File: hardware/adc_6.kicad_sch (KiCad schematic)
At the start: 12 parts, among them J5 Conn_01x04, U5 ADS122C04IPW

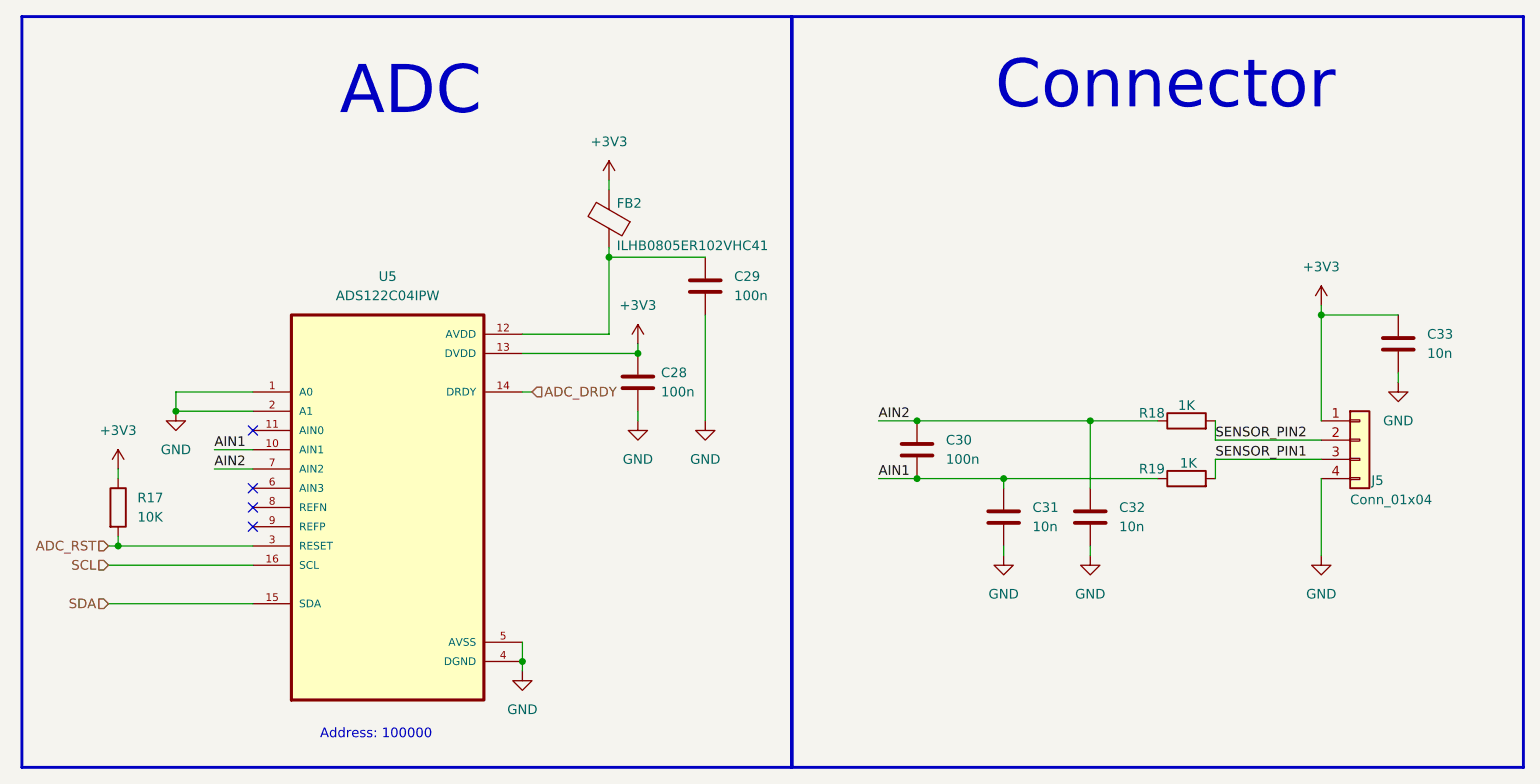
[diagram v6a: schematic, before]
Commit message: Route Ethernet section and add global labels
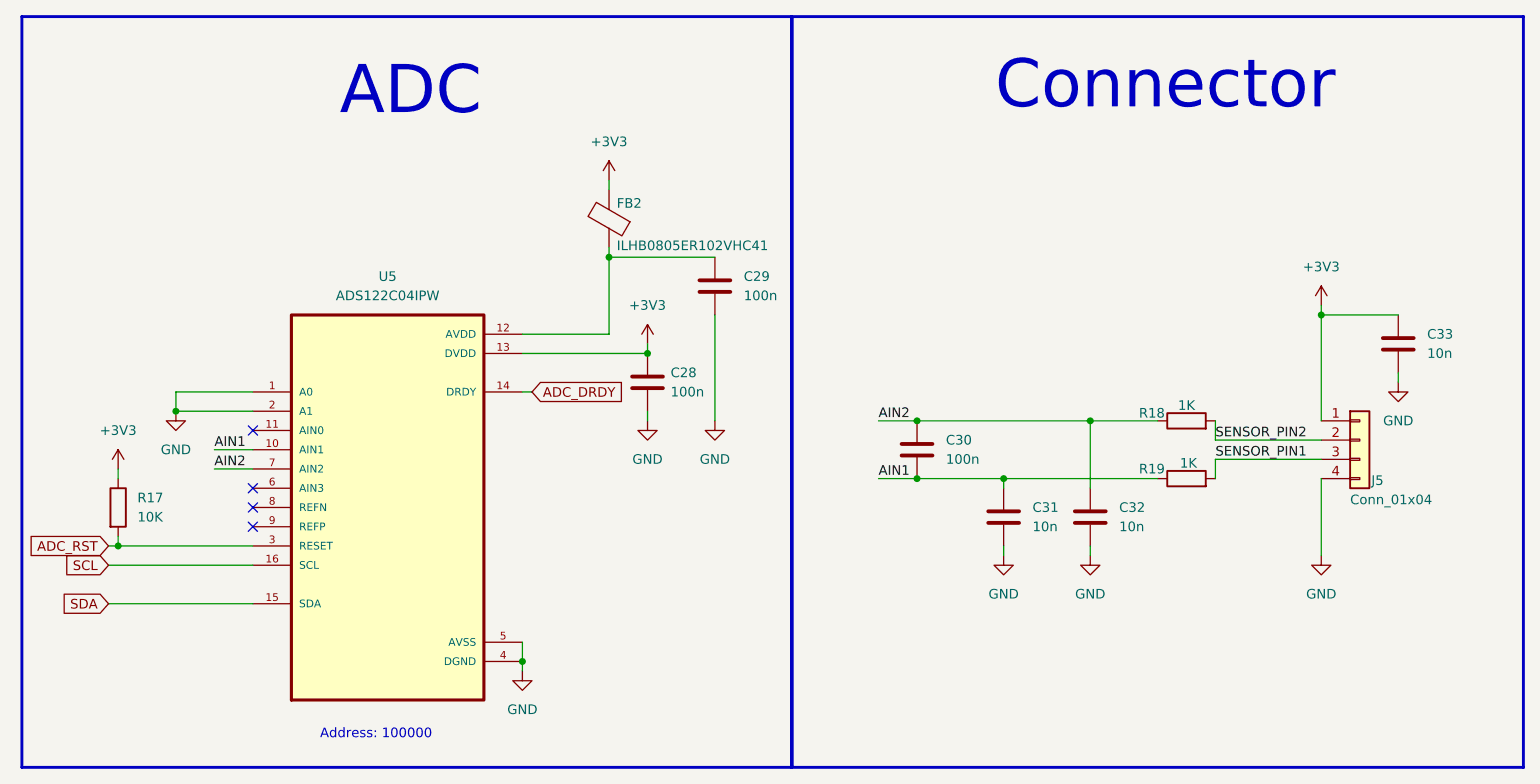
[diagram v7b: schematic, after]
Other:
- moved on the sheet: C28, C29
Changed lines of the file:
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@@
 	)
 	(junction
-		(at 132.08 86.36)
+		(at 133.35 86.36)
 		(diameter 0)
 		(color 0 0 0 0)
@@
 	(wire
 		(pts
-			(xy 116.84 86.36) (xy 132.08 86.36)
+			(xy 116.84 86.36) (xy 133.35 86.36)
 		)
 		(stroke
@@
 	(wire
 		(pts
-			(xy 132.08 95.25) (xy 132.08 93.98)
+			(xy 133.35 95.25) (xy 133.35 93.98)
 		)
 		(stroke
@@
 	(wire
 		(pts
-			(xy 128.27 73.66) (xy 140.97 73.66)
+			(xy 128.27 73.66) (xy 142.24 73.66)
 		)
 		(stroke
@@
 	(wire
 		(pts
-			(xy 140.97 95.25) (xy 140.97 81.28)
+			(xy 142.24 95.25) (xy 142.24 81.28)
 		)
 		(stroke
@@
 	(wire
 		(pts
-			(xy 132.08 85.09) (xy 132.08 86.36)
+			(xy 133.35 85.09) (xy 133.35 86.36)
 		)
 		(stroke
@@
 		)
 	)
-	(hierarchical_label "SCL"
+	(global_label "ADC_DRDY"
 		(shape input)
-		(at 62.23 114.3 180)
+		(at 118.11 91.44 0)
+		(fields_autoplaced yes)
 		(effects
 			(font
 				(size 1.27 1.27)
 			)
-			(justify right)
-		)
-	)
-	(hierarchical_label "ADC_DRDY"
+			(justify left)
+		)
+		(property "Intersheetrefs" "${INTERSHEET_REFS}"
+			(at 130.59 91.44 0)
+			(hide yes)
+			(show_name no)
+			(do_not_autoplace no)
+			(effects
+				(font
+					(size 1.27 1.27)
+				)
+				(justify left)
+			)
+		)
+	)
+	(global_label "SDA"
 		(shape input)
-		(at 118.11 91.44 0)
+		(at 62.23 119.38 180)
+		(fields_autoplaced yes)
 		(effects
 			(font
 				(size 1.27 1.27)
 			)
-			(justify left)
-		)
-	)
-	(hierarchical_label "SDA"
+			(justify right)
+		)
+		(property "Intersheetrefs" "${INTERSHEET_REFS}"
+			(at 55.6767 119.38 0)
+			(hide yes)
+			(show_name no)
+			(do_not_autoplace no)
+			(effects
+				(font
+					(size 1.27 1.27)
+				)
+				(justify right)
+			)
+		)
+	)
+	(global_label "SCL"
 		(shape input)
-		(at 62.23 119.38 180)
+		(at 62.23 114.3 180)
+		(fields_autoplaced yes)
 		(effects
 			(font
@@
 			(justify right)
 		)
-	)
-	(hierarchical_label "ADC_RST"
+		(property "Intersheetrefs" "${INTERSHEET_REFS}"
+			(at 55.7372 114.3 0)
+			(hide yes)
+			(show_name no)
+			(do_not_autoplace no)
+			(effects
+				(font
+					(size 1.27 1.27)
+				)
+				(justify right)
+			)
+		)
+	)
+	(global_label "ADC_RST"
 		(shape input)
 		(at 62.23 111.76 180)
+		(fields_autoplaced yes)
 		(effects
 			(font
@@
 			)
 			(justify right)
+		)
+		(property "Intersheetrefs" "${INTERSHEET_REFS}"
+			(at 51.2015 111.76 0)
+			(hide yes)
+			(show_name no)
+			(do_not_autoplace no)
+			(effects
+				(font
+					(size 1.27 1.27)
+				)
+				(justify right)
+			)
 		)
 	)
@@
 	(symbol
 		(lib_id "power:GND")
-		(at 132.08 95.25 0)
+		(at 133.35 95.25 0)
 		(unit 1)
 		(body_style 1)
@@
 		(fields_autoplaced yes)
 		(property "Reference" "#PWR056"
-			(at 132.08 101.6 0)
+			(at 133.35 101.6 0)
 			(hide yes)
 			(show_name no)
@@
 		)
 		(property "Value" "GND"
-			(at 132.08 100.33 0)
+			(at 133.35 100.33 0)
 			(show_name no)
 			(do_not_autoplace no)
@@
 		)
 		(property "Footprint" ""
-			(at 132.08 95.25 0)
+			(at 133.35 95.25 0)
 			(hide yes)
 			(show_name no)
@@
 		)
 		(property "Datasheet" ""
-			(at 132.08 95.25 0)
+			(at 133.35 95.25 0)
 			(hide yes)
 			(show_name no)
@@
 		)
 		(property "Description" "Power symbol creates a global label with name \"GND\" , ground"
-			(at 132.08 95.25 0)
+			(at 133.35 95.25 0)
 			(hide yes)
 			(show_name no)
@@
 	(symbol
 		(lib_id "power:+3V3")
-		(at 132.08 85.09 0)
+		(at 133.35 85.09 0)
 		(unit 1)
 		(body_style 1)
@@
 		(fields_autoplaced yes)
 		(property "Reference" "#PWR055"
-			(at 132.08 88.9 0)
+			(at 133.35 88.9 0)
 			(hide yes)
 			(show_name no)
@@
 		)
 		(property "Value" "+3V3"
-			(at 132.08 80.01 0)
+			(at 133.35 80.01 0)
 			(show_name no)
 			(do_not_autoplace no)
@@
 		)
 		(property "Footprint" ""
-			(at 132.08 85.09 0)
+			(at 133.35 85.09 0)
 			(hide yes)
 			(show_name no)
@@
 		)
 		(property "Datasheet" ""
-			(at 132.08 85.09 0)
+			(at 133.35 85.09 0)
 			(hide yes)
 			(show_name no)
@@
 		)
 		(property "Description" "Power symbol creates a global label with name \"+3V3\""
-			(at 132.08 85.09 0)
+			(at 133.35 85.09 0)
 			(hide yes)
 			(show_name no)
@@
 	(symbol
 		(lib_id "Device:C")
-		(at 140.97 77.47 0)
+		(at 142.24 77.47 0)
 		(unit 1)
 		(body_style 1)
@@
 		(fields_autoplaced yes)
 		(property "Reference" "C29"
-			(at 144.78 76.1999 0)
+			(at 146.05 76.1999 0)
 			(show_name no)
 			(do_not_autoplace no)
@@
 		)
 		(property "Value" "100n"
-			(at 144.78 78.7399 0)
+			(at 146.05 78.7399 0)
 			(show_name no)
 			(do_not_autoplace no)
@@
 		)
 		(property "Footprint" "STM32F407 Dev Kit Library:C_0805_2012Metric_Pad1.18x1.45mm_HandSolder"
-			(at 141.9352 81.28 0)
+			(at 143.2052 81.28 0)
 			(hide yes)
 			(show_name no)
@@
 		)
 		(property "Datasheet" ""
-			(at 140.97 77.47 0)
+			(at 142.24 77.47 0)
 			(hide yes)
 			(show_name no)
@@
 		)
 		(property "Description" "Unpolarized capacitor"
-			(at 140.97 77.47 0)
+			(at 142.24 77.47 0)
 			(hide yes)
 			(show_name no)
@@
 	(symbol
 		(lib_id "Device:C")
-		(at 132.08 90.17 0)
+		(at 133.35 90.17 0)
 		(unit 1)
 		(body_style 1)
@@
 		(dnp no)
 		(property "Reference" "C28"
-			(at 135.128 88.9 0)
+			(at 136.398 88.9 0)
 			(show_name no)
 			(do_not_autoplace no)
@@
 		)
 		(property "Value" "100n"
-			(at 135.128 91.44 0)
+			(at 136.398 91.44 0)
 			(show_name no)
 			(do_not_autoplace no)
@@
 		)
 		(property "Footprint" "STM32F407 Dev Kit Library:C_0805_2012Metric_Pad1.18x1.45mm_HandSolder"
-			(at 133.0452 93.98 0)
+			(at 134.3152 93.98 0)
 			(hide yes)
 			(show_name no)
@@
 		)
 		(property "Datasheet" ""
-			(at 132.08 90.17 0)
+			(at 133.35 90.17 0)
 			(hide yes)
 			(show_name no)
@@
 		)
 		(property "Description" "Unpolarized capacitor"
-			(at 132.08 90.17 0)
+			(at 133.35 90.17 0)
 			(hide yes)
 			(show_name no)
@@
 	(symbol
 		(lib_id "power:GND")
-		(at 140.97 95.25 0)
+		(at 142.24 95.25 0)
 		(unit 1)
 		(body_style 1)
@@
 		(fields_autoplaced yes)
 		(property "Reference" "#PWR057"
-			(at 140.97 101.6 0)
+			(at 142.24 101.6 0)
 			(hide yes)
 			(show_name no)
@@
 		)
 		(property "Value" "GND"
-			(at 140.97 100.33 0)
+			(at 142.24 100.33 0)
 			(show_name no)
 			(do_not_autoplace no)
@@
 		)
 		(property "Footprint" ""
-			(at 140.97 95.25 0)
+			(at 142.24 95.25 0)
 			(hide yes)
 			(show_name no)
@@
 		)
 		(property "Datasheet" ""
-			(at 140.97 95.25 0)
+			(at 142.24 95.25 0)
 			(hide yes)
 			(show_name no)
@@
 		)
 		(property "Description" "Power symbol creates a global label with name \"GND\" , ground"
-			(at 140.97 95.25 0)
-			(hide yes)
-			(show_name no)
+			(at 142.24 95.25 0)
+			(hide yes)
+			(show_name no)
